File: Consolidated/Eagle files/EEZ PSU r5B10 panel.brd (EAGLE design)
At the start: 309 x 150 mm, 838 parts, among them IC1 LTC3864EMSE#PBF, IC10 REF5025AIDG4, IC11 DAC8552IDGKTG4, IC12 ADG465SOT-23, IC13 TS5A9411DCKT, IC14 ADS1120IPWR, IC15 LP339D, IC16 LM25575MH/NOPB, IC17 TPD4E002DRLR, IC18 TPD2E001DZDR, IC19 ADUM3160BRWZ, IC2 MC79L05, IC20 TLC5925IDBQR, IC21 Si8641EC-B-IS1, IC22 SI8651EC-B-IS1, IC23 SI8651EC-B-IS1, IC24 LD1117ADT33TR, IC25 Si8641EC-B-IS1, IC26 PCA21125T/Q900/1,1, IC27 AT25256B-SSHL-B, IC28 W5500, IC29 BC857BS, IC3 MC78L05, IC30 TLC555, IC31 SN74LVC2G08DCTR, IC32 TPS3705-33D, IC33 SN74LV1T34DBVR, IC34 SN74LVC2G02DCTR, IC35 DAC8552IDGKTG4, IC36 ADS1120IPWR, IC37 MCP23S08-E/SO, IC38 OP27GSZ, IC39 TL072D, IC4 LM5574MTX/NOPB, IC40 TL072D, IC41 REF5025AIDG4, IC42 LTC3864EMSE#PBF, IC43 LM5574MTX/NOPB, IC44 MC79L05, IC45 MC78L05, IC46 TS5A9411DCKT, IC47 ADG465SOT-23, IC48 LP339D, IC49 LP2951SO8, IC5 LP2951SO8, IC6 TL072D, IC7 TL072D, IC8 OP27GSZ, IC9 MCP23S08-E/SO, J1 BS-244DSM-R, J2 BS-244DSM-G, J3 BS-244DSM-B, J4 BS-244DSM-R, J5 BS-244DSM-B, Q1 IRFR5305, Q10 MMBT5401, Q11 MMBT5401, Q12 MMBT5551, Q13 MMBT5551, Q14 BSS84P, Q15 2N7002, Q16 MMBT5551, Q17 MMBT5401, Q18 MMBT5551, Q19 MMBT5551, Q2 MMBT5401, Q20 BTA26-600, Q21 BTA26-600, Q22 IRLL014N, Q23 IRLML2246TRPBF, Q24 IRLML2246TRPBF, Q25 IRLML2246TRPBF, Q26 IRLML2246TRPBF, Q27 2N7002, Q28 IRLML2246TRPBF, Q29 2N7002, Q3 2N7002, Q30 2N7002, Q31 IRFP250N, Q32 BCP56-16.115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

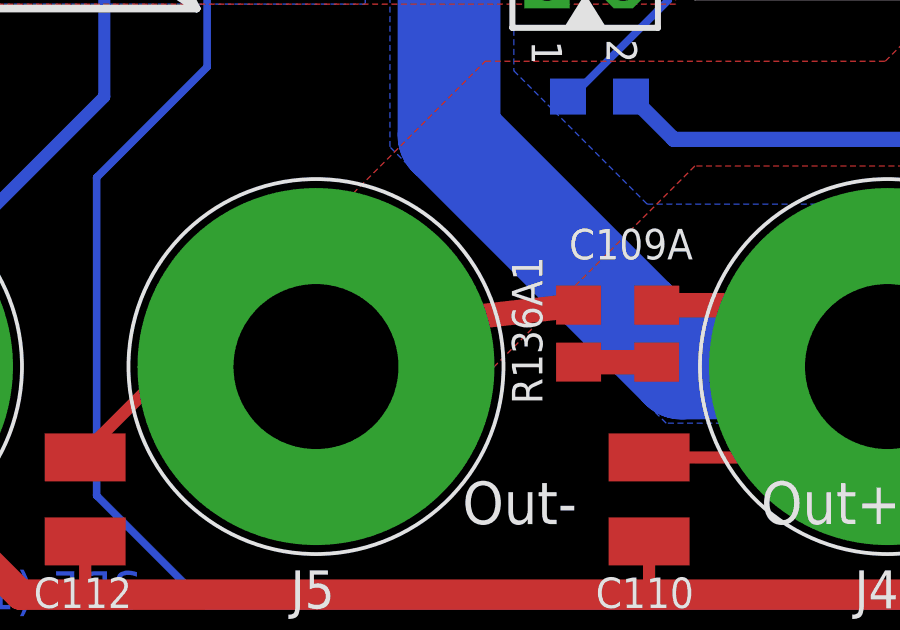
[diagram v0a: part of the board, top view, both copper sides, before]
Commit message: r5B10 BOM, top silkscreen minor correction
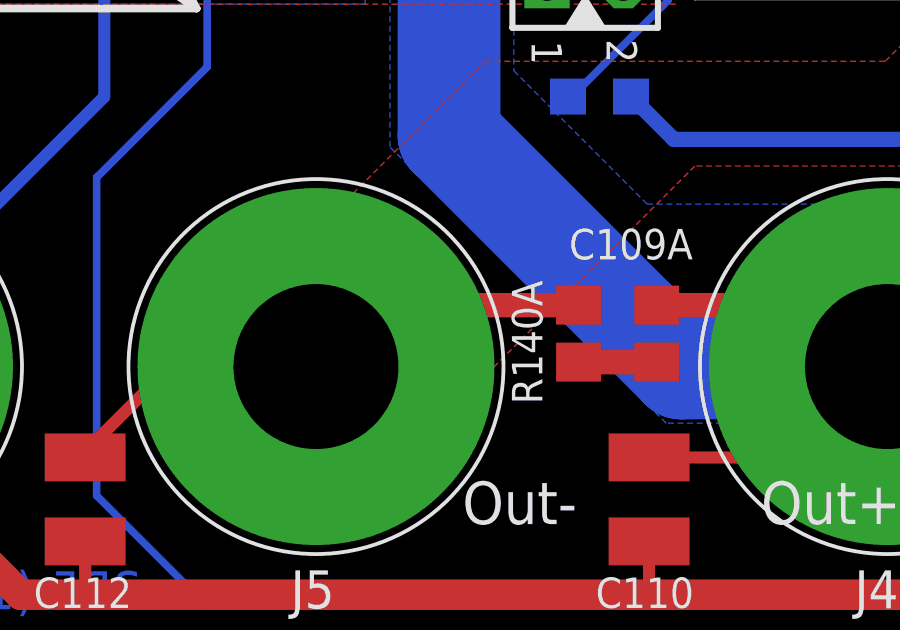
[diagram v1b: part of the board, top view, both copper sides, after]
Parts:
- renumbered R136A1 to R140A
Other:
- board text added: "R140A"
- board text removed: "R136A1"
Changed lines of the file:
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@@
 <layer number="21" name="tPlace" color="7" fill="1" visible="yes" active="yes"/>
 <layer number="22" name="bPlace" color="13" fill="1" visible="no" active="yes"/>
-<layer number="23" name="tOrigins" color="15" fill="1" visible="no" active="yes"/>
+<layer number="23" name="tOrigins" color="15" fill="1" visible="yes" active="yes"/>
 <layer number="24" name="bOrigins" color="15" fill="1" visible="no" active="yes"/>
 <layer number="25" name="tNames" color="7" fill="1" visible="no" active="yes"/>
@@
 <board>
 <plain>
+<dimension x1="309" y1="0" x2="0" y2="-1" x3="154.5" y3="-6.5" layer="113" dtype="horizontal"/>
+<dimension x1="0" y1="0" x2="0" y2="150" x3="-5.5" y3="75" layer="113" dtype="vertical"/>
 <wire x1="1.5" y1="76" x2="148.5" y2="76" width="0.1" layer="20"/>
 <wire x1="0" y1="148.5" x2="0" y2="77.5" width="0.1" layer="20"/>
@@
 <text x="176.7055" y="28.1305" size="1.016" layer="125" ratio="10">R136</text>
 <text x="172.959" y="7.62" size="1.016" layer="125" ratio="10" rot="R90">R136A</text>
-<text x="134.097" y="7.747" size="1.016" layer="125" ratio="10" rot="R90">R136A1</text>
+<text x="134.097" y="7.747" size="1.016" layer="125" ratio="10" rot="R90">R140A</text>
 <text x="151.26389375" y="52.269390625" size="0.9906" layer="125" ratio="10">R137</text>
 <text x="156.5394" y="67.20489375" size="0.9906" layer="125" ratio="10">R138</text>
@@
 <text x="203.801" y="77.2795" size="1.016" layer="125" ratio="10">ZD4</text>
 <text x="206.7855" y="100.076" size="1.016" layer="125" ratio="10" rot="R270">ZD5</text>
-<dimension x1="309" y1="0" x2="0" y2="-1" x3="154.5" y3="-6.5" layer="113" dtype="horizontal"/>
-<dimension x1="0" y1="0" x2="0" y2="150" x3="-5.5" y3="75" layer="113" dtype="vertical"/>
 </plain>
 <attributes>
@@
 <attribute name="VALUE" x="137.2085" y="11.3665" size="1.27" layer="27" rot="R270"/>
 </element>
-<element name="R136A1" library="rcl" package="R0805" value="1R" x="135.3035" y="10.0965" smashed="yes" rot="R270">
+<element name="R140A" library="rcl" package="R0805" value="1R" x="135.3035" y="10.0965" smashed="yes" rot="R270">
 <attribute name="NAME" x="134.097" y="7.747" size="1.016" layer="25" ratio="10" rot="R90"/>
 <attribute name="VALUE" x="134.732" y="11.43" size="1.27" layer="27" rot="R270"/>
@@
 <contactref element="C112" pad="2"/>
 <wire x1="118.857" y1="5.972" x2="118.4125" y2="5.718" width="0.4064" layer="1"/>
-<contactref element="R136A1" pad="1"/>
-<wire x1="135.3035" y1="11.0465" x2="127.4905" y2="10.1575" width="0.8128" layer="1"/>
-<wire x1="127.4905" y1="10.1575" x2="126.731" y2="9.398" width="0.8128" layer="1"/>
+<contactref element="R140A" pad="1"/>
+<wire x1="135.3035" y1="11.0465" x2="128.3795" y2="11.0465" width="0.8128" layer="1"/>
+<wire x1="128.3795" y1="11.0465" x2="126.731" y2="9.398" width="0.8128" layer="1"/>
 </signal>
 <signal name="N$306">
@@
 <wire x1="179.563" y1="47.6885" x2="178.42" y2="48.8315" width="0.254" layer="1"/>
 <wire x1="201.407" y1="46.9265" x2="203.439" y2="48.9585" width="0.254" layer="1"/>
-<wire x1="204.0105" y1="48.9585" x2="204.0486" y2="48.9585" width="0" layer="19" extent="1-1"/>
-<wire x1="175.252" y1="42.15" x2="175.245" y2="42.164" width="0" layer="19" extent="16-16"/>
+<wire x1="175.245" y1="42.164" x2="175.252" y2="42.15" width="0" layer="19" extent="16-16"/>
+<wire x1="204.0486" y1="48.9585" x2="204.0105" y2="48.9585" width="0" layer="19" extent="1-1"/>
 </signal>
 <signal name="!CH1_DAC">
@@
 <signal name="N$178">
 <contactref element="C109A" pad="2"/>
-<contactref element="R136A1" pad="2"/>
+<contactref element="R140A" pad="2"/>
 <wire x1="135.3035" y1="9.1465" x2="137.907" y2="9.1465" width="0.8128" layer="1"/>
 </signal>
@@
 <wire x1="128.321" y1="80.391" x2="122.9845" y2="80.391" width="0.6096" layer="1"/>
 <wire x1="122.9845" y1="80.391" x2="122.6035" y2="80.01" width="0.6096" layer="1"/>
-<wire x1="122.6035" y1="80.01" x2="122.5" y2="80" width="0" layer="19" extent="1-1"/>
+<wire x1="122.5" y1="80" x2="122.6035" y2="80.01" width="0" layer="19" extent="1-1"/>
 </signal>
 <signal name="N$182">
@@
 <wire x1="186.275" y1="92.9005" x2="186.2565" y2="92.9015" width="0" layer="19" extent="1-1"/>
 <wire x1="221.8655" y1="133.1265" x2="221.8985" y2="133.1595" width="0" layer="19" extent="1-1"/>
+<wire x1="179.6075" y1="71.12" x2="171.289" y2="84.6455" width="0" layer="19" extent="1-1"/>
 </signal>
 <signal name="+5V1">
@@
 <wire x1="164.512" y1="131.399" x2="164.685" y2="131.572" width="0.254" layer="1"/>
 <wire x1="164.685" y1="131.572" x2="164.6215" y2="131.572" width="0.254" layer="1"/>
-<wire x1="164.6215" y1="131.572" x2="164.624" y2="131.572" width="0" layer="19" extent="1-1"/>
+<wire x1="223.105" y1="102.362" x2="245.33" y2="61.5975" width="0" layer="19" extent="1-1"/>
+<wire x1="164.624" y1="131.572" x2="164.6215" y2="131.572" width="0" layer="19" extent="1-1"/>
 </signal>
 <signal name="PREG_OUT1">
@@
 <wire x1="286.986" y1="100.838" x2="289.142" y2="100.838" width="0.6096" layer="1"/>
 <wire x1="289.142" y1="100.838" x2="289.145" y2="100.835" width="0.4064" layer="1"/>
+<wire x1="282.221" y1="80.391" x2="266" y2="39.08" width="0" layer="19" extent="1-1"/>
 </signal>
 <signal name="N$267">
@@
 <wire x1="280.321" y1="80.391" x2="274.9845" y2="80.391" width="0.6096" layer="1"/>
 <wire x1="274.9845" y1="80.391" x2="274.6035" y2="80.01" width="0.6096" layer="1"/>
-<wire x1="274.6035" y1="80.01" x2="274.5" y2="80" width="0" layer="19" extent="1-1"/>
+<wire x1="274.5" y1="80" x2="274.6035" y2="80.01" width="0" layer="19" extent="1-1"/>
 </signal>
 <signal name="N$276">
